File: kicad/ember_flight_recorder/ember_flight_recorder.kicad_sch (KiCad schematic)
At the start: 18 parts, among them Q3 FS8205A, Q4 AO3401A, U1 ESP32-C3-SuperMini, U2 DW01A, U3 MCP1700x-330xxTT, U4 module_mpu6050, U5 module_bme280

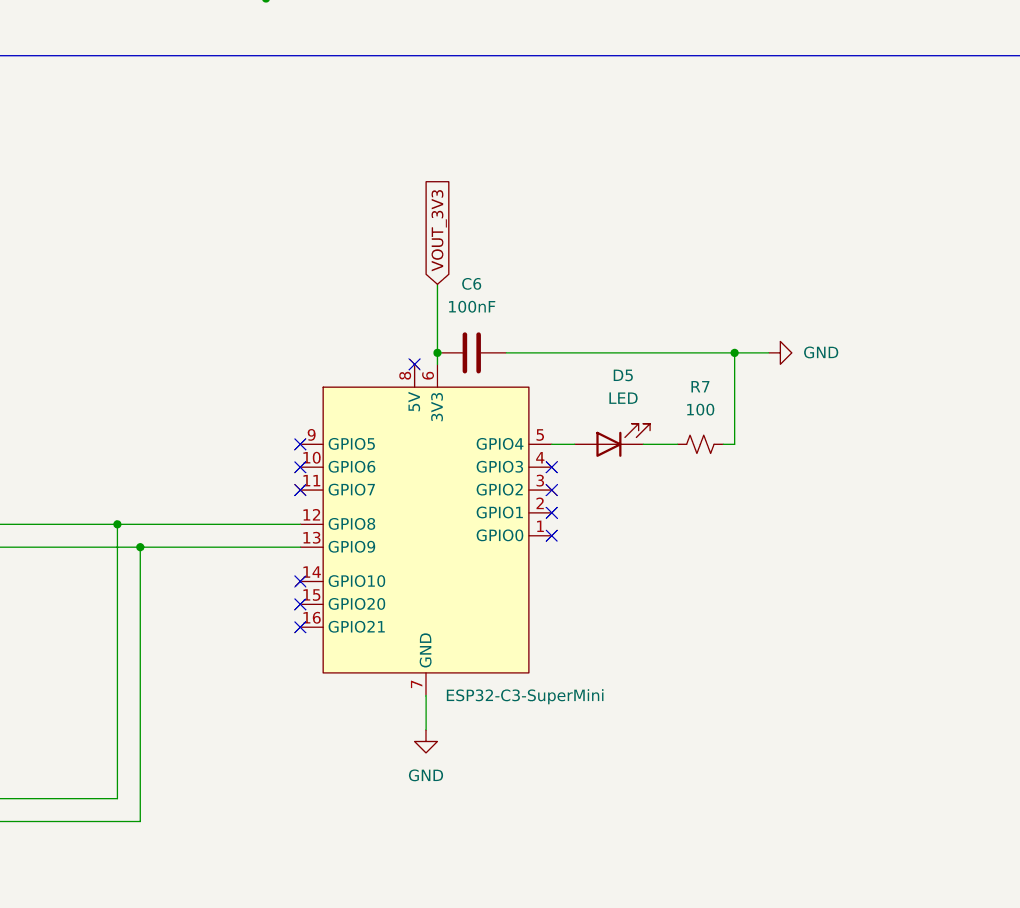
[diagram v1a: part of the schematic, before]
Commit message: updated footprint and 3d models
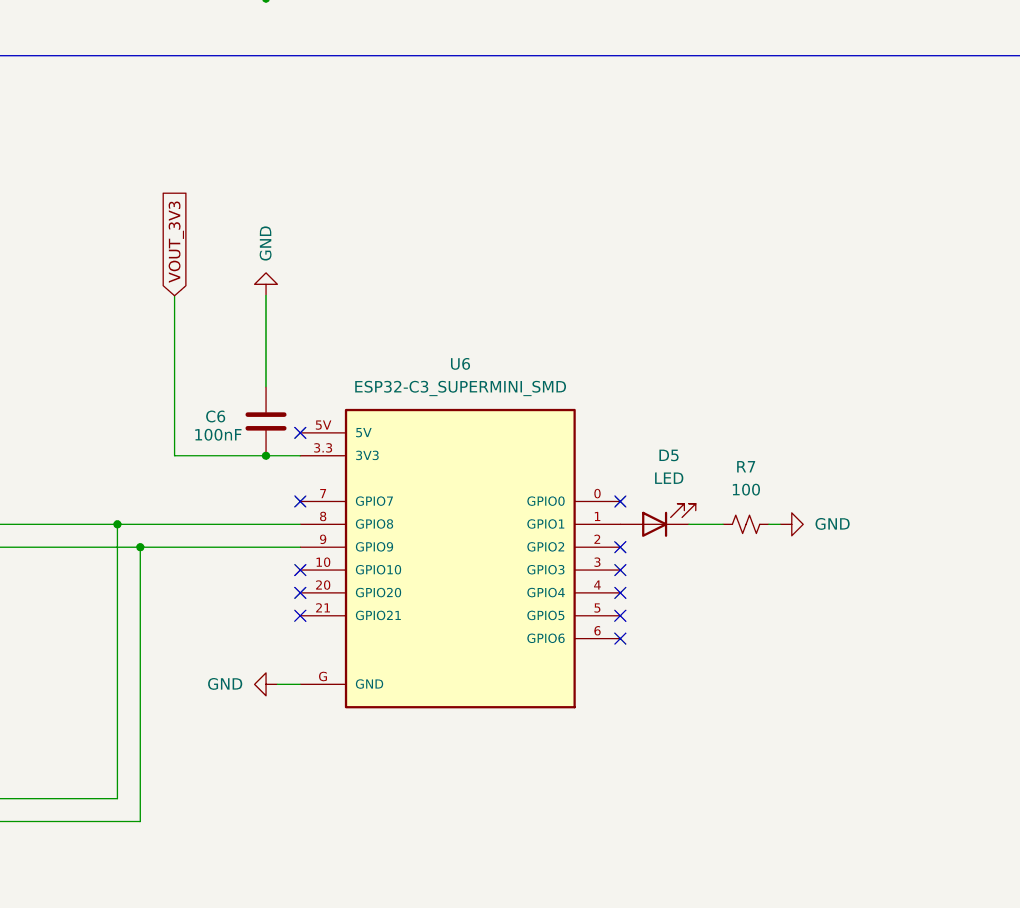
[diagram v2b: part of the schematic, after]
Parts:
- removed U1: ESP32-C3-SuperMini, ESP32-C3-SuperMini:ESP32-C3-SuperMini, symbol ESP32-C3-SuperMini:ESP32-C3-SuperMini
- added U6: ESP32-C3_SUPERMINI_SMD, smd:MODULE_ESP32-C3_SUPERMINI, symbol ESP32-C3_SUPERMINI_SMD:ESP32-C3_SUPERMINI_SMD
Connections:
- net GND: now also U6.G (GND)
- net VOUT_3V3: now also U6.3.3 (3V3)
- net at U4.3 (SCL), U5.3 (SCL): now also U6.9 (GPIO9)
- net at U4.4 (SDA), U5.4 (SDA): now also U6.8 (GPIO8)
- net at D5.2 (A): now also U6.1 (GPIO1)
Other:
- moved on the sheet: C6, D5, R7

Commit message: flight recorder rev1
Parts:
- added SW1: SW_SPDT, Button_Switch_THT:SW_Slide-03_Wuerth-WS-SLTV_10x2.5x6.4_P2.54mm, symbol Switch:SW_SPDT
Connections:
- net GND: no longer BT1.2 (-), C1.2, Q3.1, Q4.1 (G), U2.6 (GND)
- net at U6.1 (GPIO1): no longer D5.2 (A)
- net at U6.10 (GPIO10): now also D5.2 (A)
- new net: C1.2, Q3.1, SW1.3 (C), U2.6 (GND)
- new net GNDPWR: BT1.2 (-), Q4.1 (G), SW1.2 (B)
- no-connect marks 16 -> 17
